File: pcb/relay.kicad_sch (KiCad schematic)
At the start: 14 parts, among them K1 PR24-5V-900-1A, P1 MountingHole_Pad, P2 MountingHole_Pad, P3 MountingHole_Pad, P4 MountingHole_Pad, Q1 MMBT3904, U3 LTV-356T

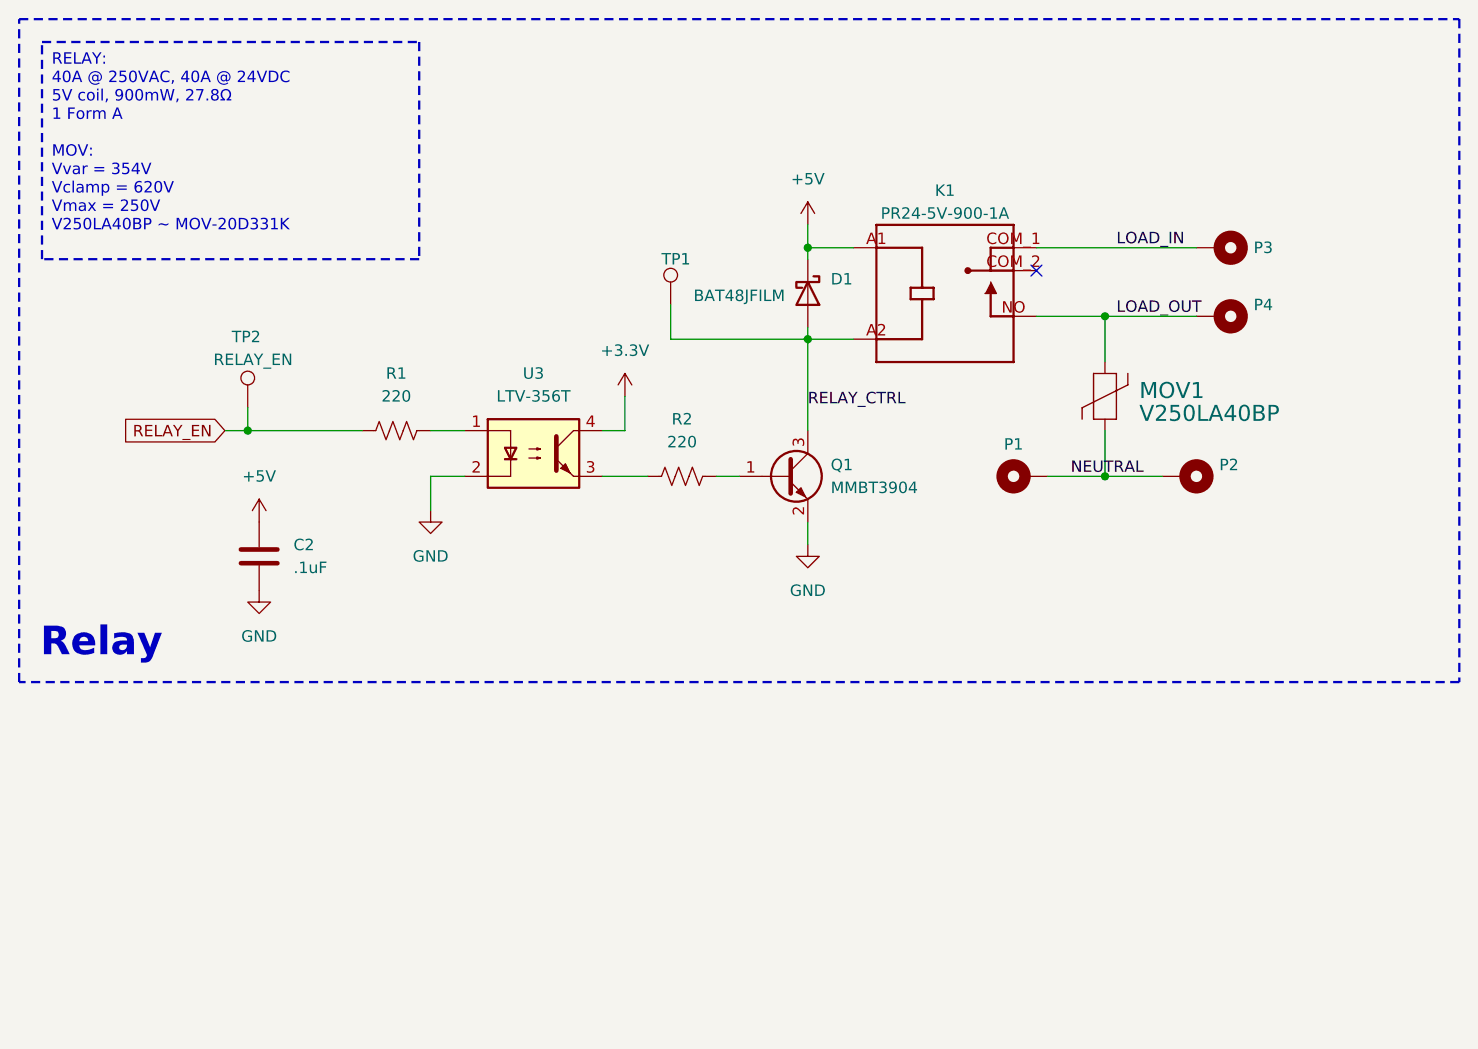
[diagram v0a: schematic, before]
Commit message: Updated to latest libraries
Changed to all CRG footprints (mostly)
Moved somethings around
Added LED jumper
Updated symbols/logos
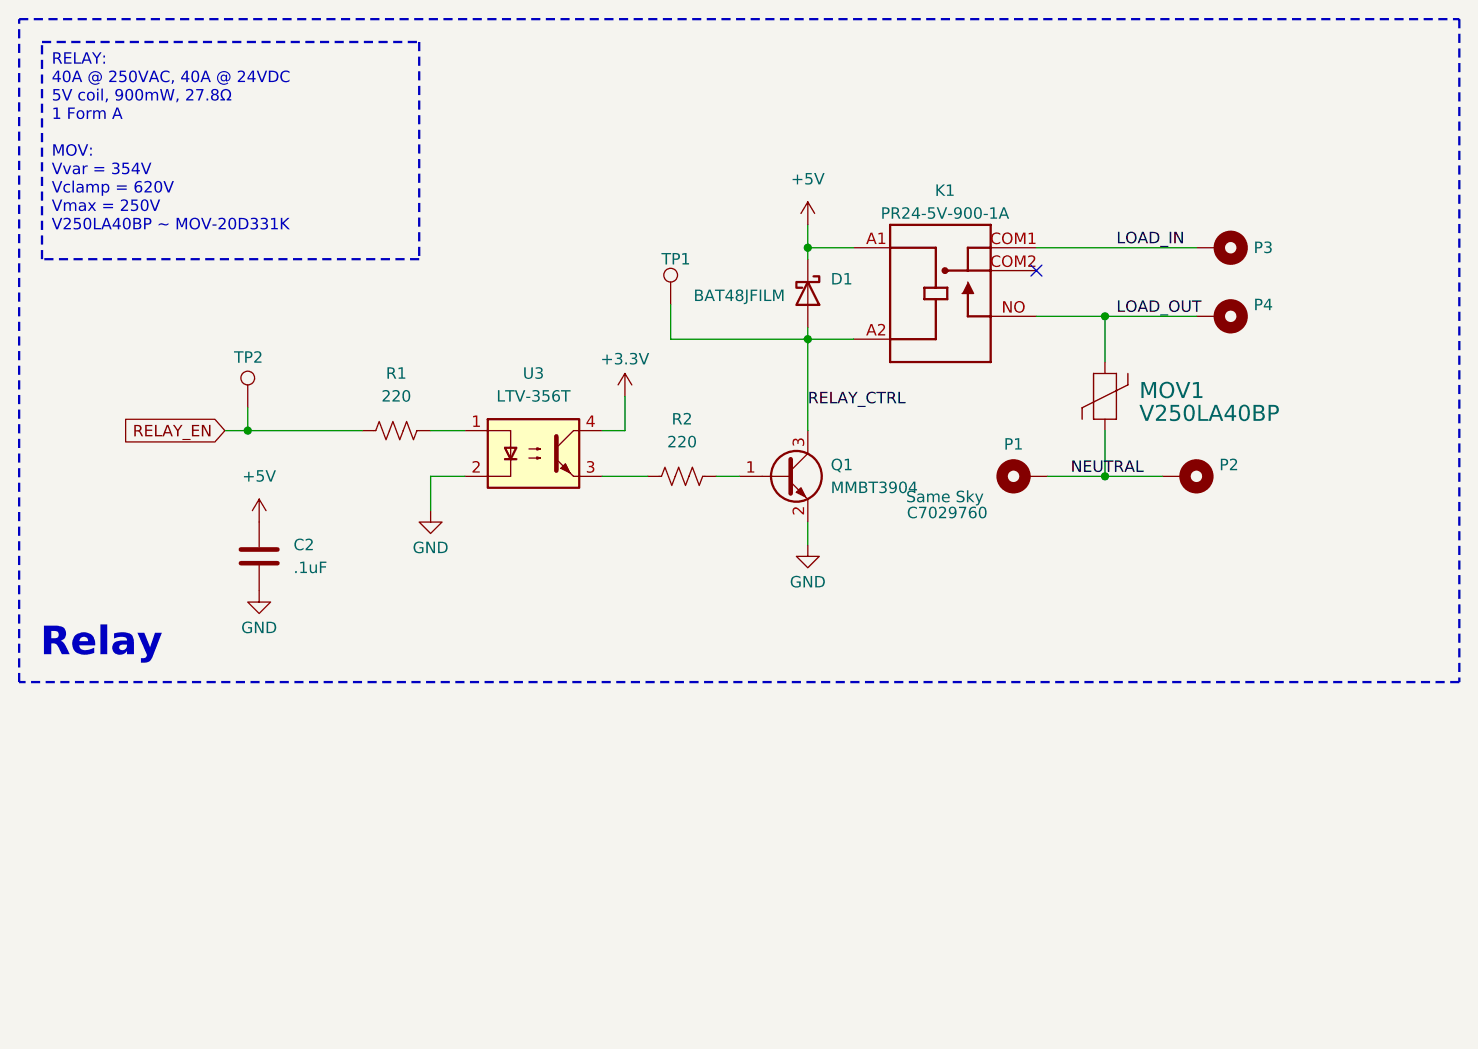
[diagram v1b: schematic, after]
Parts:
- C2: footprint Capacitor_SMD:C_0603_1608Metric -> CRGM Passive:C_0603_1608Metric; Digikey (none) -> 1276-1860-2-ND; Mouser (none) -> 187-CL10A105KB8NNNC
- D1: footprint Diode_SMD:D_SOD-323 -> CRG Makes:SOD-323; Digikey (none) -> 497-5711-2-ND; Mouser (none) -> 511-BAT48JFILM
- Q1: footprint Package_TO_SOT_SMD:SOT-23 -> CRGM Passive:SOT-23; Digikey (none) -> 3372-MMBT3904TR-ND; Mouser (none) -> 637-MMBT3904
- R1, R2: footprint Resistor_SMD:R_0603_1608Metric -> CRGM Passive:R_0603_1608Metric
- TP1: value RELAY_CTRL -> ~; symbol Connector:TestPoint -> CRGM Connector:TestPoint
- TP2: value RELAY_EN -> ~; symbol Connector:TestPoint -> CRGM Connector:TestPoint
- U3: Digikey (none) -> 160-1337-2-ND; Mouser (none) -> 859-LTV-356T
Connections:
- net LOAD_IN: now also K1.COM1; no longer K1.COM_1 (COM1)

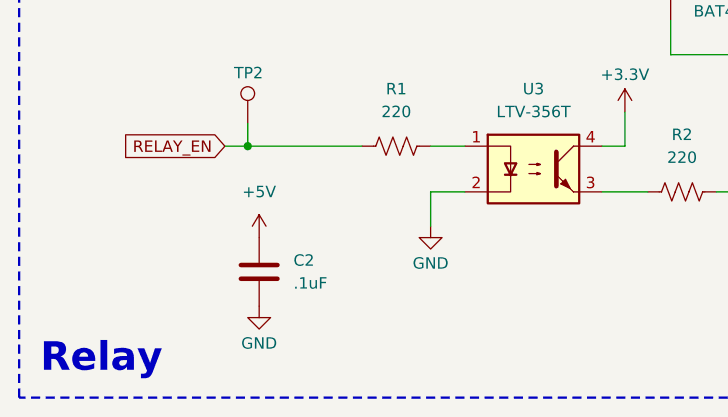
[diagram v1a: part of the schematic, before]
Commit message: Fixed capacitor attributes
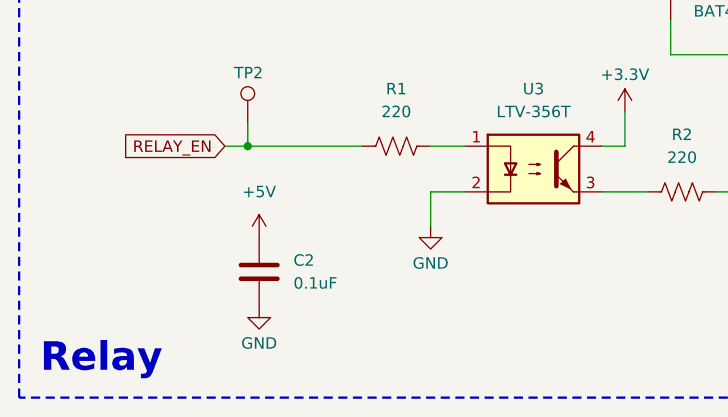
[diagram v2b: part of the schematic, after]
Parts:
- C2: value .1uF -> 0.1uF; Digikey 1276-1860-2-ND -> 1276-1005-2-ND; LCSC C15849 -> C66501; MPN CL10A105KB8NNNC -> CL10B104KO8NNNC; Mouser 187-CL10A105KB8NNNC -> 187-CL10B104KO8NNNC; Tolerance (none) -> 10%; Vr (none) -> 16V
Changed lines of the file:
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@@
 			)
 		)
-		(property "Value" ".1uF"
+		(property "Value" "0.1uF"
 			(at 45.72 76.1999 0)
 			(effects
@@
 			)
 		)
-		(property "MPN" "CL10A105KB8NNNC"
+		(property "MPN" "CL10B104KO8NNNC"
 			(at 41.91 74.93 0)
 			(effects
@@
 			)
 		)
-		(property "Digikey" "1276-1860-2-ND"
+		(property "LCSC" "C66501"
 			(at 41.91 74.93 0)
 			(effects
@@
 			)
 		)
-		(property "Mouser" "187-CL10A105KB8NNNC"
+		(property "Digikey" "1276-1005-2-ND"
 			(at 41.91 74.93 0)
 			(effects
@@
 			)
 		)
-		(property "LCSC" "C15849"
+		(property "Mouser" "187-CL10B104KO8NNNC"
 			(at 41.91 74.93 0)
 			(effects
@@
 			)
 		)
-		(property "Sim.Enable" ""
+		(property "Tolerance" "10%"
+			(at 41.91 74.93 0)
+			(effects
+				(font
+					(size 1.27 1.27)
+				)
+				(hide yes)
+			)
+		)
+		(property "Vr" "16V"
 			(at 41.91 74.93 0)
 			(effects
@@
 			)
 		)
-		(property "Sim.Enable" ""
-			(at 148.59 40.64 90)
-			(effects
-				(font
-					(size 1.27 1.27)
-				)
-				(hide yes)
-			)
-		)
 		(pin "1"
 		)
@@
 					(size 1.27 1.27)
 				)
-			)
-		)
-		(property "Sim.Enable" ""
-			(at 118.11 45.72 0)
-			(effects
-				(font
-					(size 1.27 1.27)
-				)
-				(hide yes)
 			)
 		)
@@
 			)
 		)
-		(property "Sim.Enable" ""
-			(at 72.39 63.5 0)
-			(effects
-				(font
-					(size 1.27 1.27)
-				)
-				(hide yes)
-			)
-		)
 		(pin "1"
 		)
@@
 			)
 		)
-		(property "Sim.Enable" ""
-			(at 135.89 57.15 0)
-			(effects
-				(font
-					(size 1.27 1.27)
-				)
-				(hide yes)
-			)
-		)
 		(pin "P$1"
 		)
@@
 		(property "Description" "Test Point D1.0mm"
 			(at 40.64 67.564 0)
-			(effects
-				(font
-					(size 1.27 1.27)
-				)
-				(hide yes)
-			)
-		)
-		(property "Sim.Enable" ""
-			(at 40.64 58.42 0)
 			(effects
 				(font
@@
 			)
 		)
-		(property "Sim.Enable" ""
-			(at 148.59 48.26 90)
-			(effects
-				(font
-					(size 1.27 1.27)
-				)
-				(hide yes)
-			)
-		)
 		(pin "1"
 		)
@@
 			)
 		)
-		(property "Sim.Enable" ""
-			(at 57.15 60.96 90)
-			(effects
-				(font
-					(size 1.27 1.27)
-				)
-				(hide yes)
-			)
-		)
 		(pin "2"
 		)
@@
 			)
 		)
-		(property "Sim.Enable" ""
-			(at 100.33 66.04 0)
-			(effects
-				(font
-					(size 1.27 1.27)
-				)
-				(hide yes)
-			)
-		)
 		(pin "3"
 		)
@@
 		(property "MN" "STMicroelectronics"
 			(at 102.87 45.72 0)
-			(effects
-				(font
-					(size 1.27 1.27)
-				)
-				(hide yes)
-			)
-		)
-		(property "Sim.Enable" ""
-			(at 102.87 45.72 90)
 			(effects
 				(font
@@
 			)
 		)
-		(property "Sim.Enable" ""
-			(at 88.9 66.04 90)
-			(effects
-				(font
-					(size 1.27 1.27)
-				)
-				(hide yes)
-			)
-		)
 		(pin "2"
 		)
@@
 			)
 		)
-		(property "Sim.Enable" ""
-			(at 127 66.04 90)
-			(effects
-				(font
-					(size 1.27 1.27)
-				)
-				(hide yes)
-			)
-		)
 		(pin "1"
 		)
@@
 			)
 		)
-		(property "Sim.Enable" ""
-			(at 144.78 66.04 90)
-			(effects
-				(font
-					(size 1.27 1.27)
-				)
-				(hide yes)
-			)
-		)
 		(pin "1"
 		)
@@
 			(effects
 				(font
-					(size 1.27 1.27)
-				)
-				(hide yes)
-			)
-		)
-		(property "Sim.Enable" ""
-			(at 87.63 46.99 0)
-			(effects
-				(font

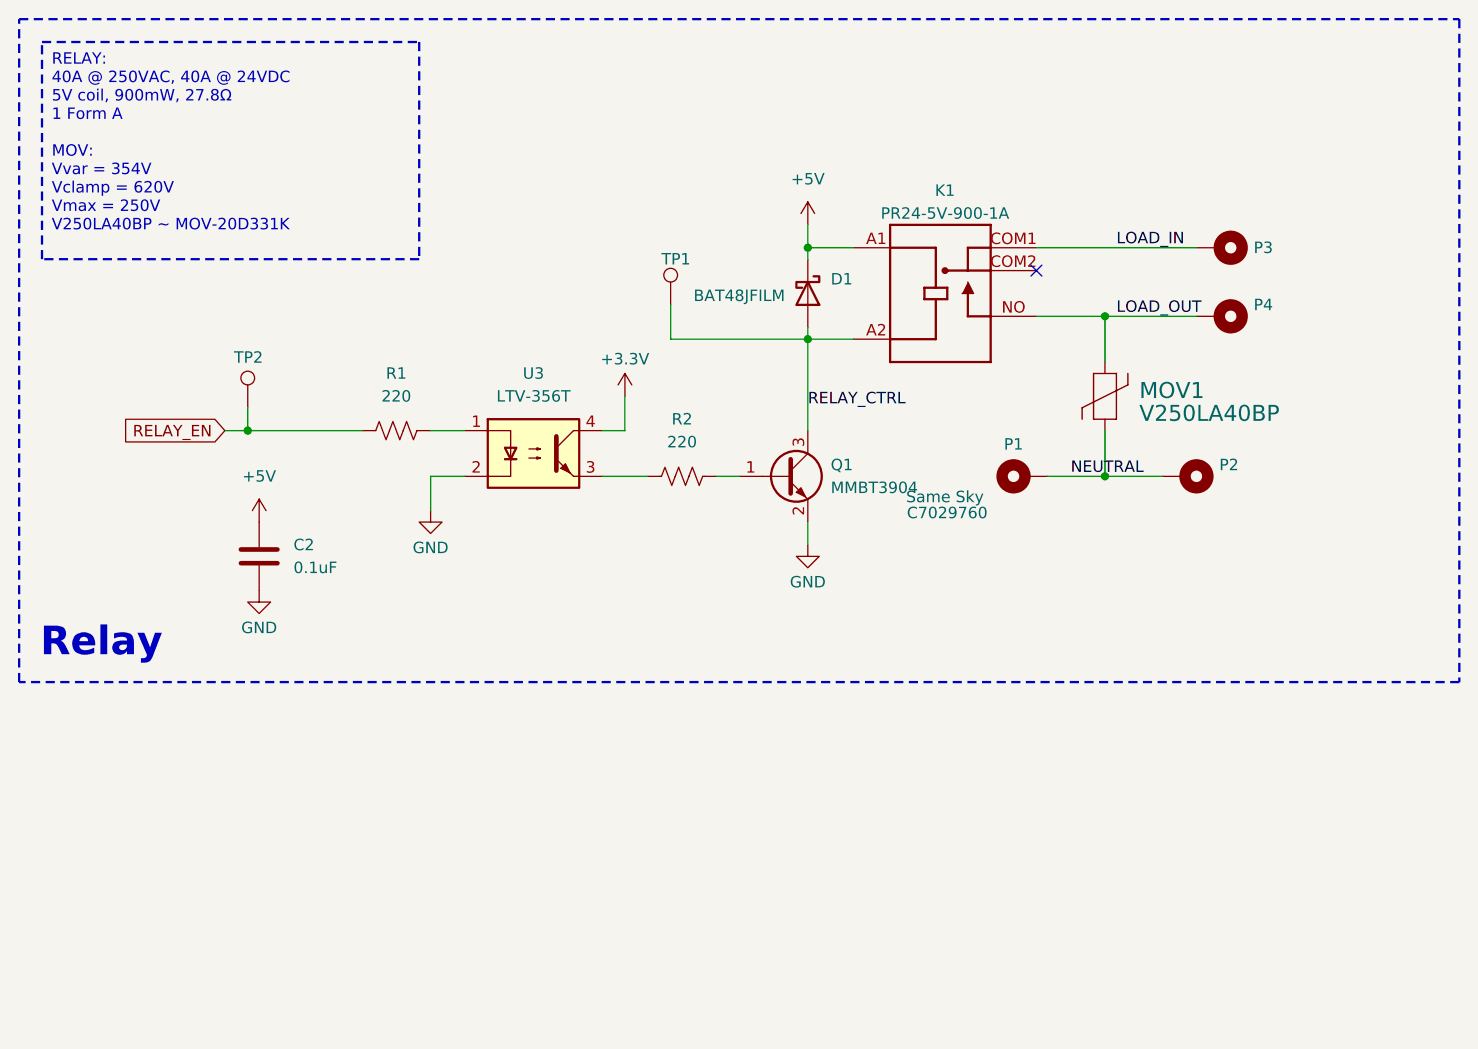
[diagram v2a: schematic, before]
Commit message: Updated for consistency
Updated footprints
Added ESD to power
Added second QWICC connector
Rerouted as required
Made mounting holes grounded
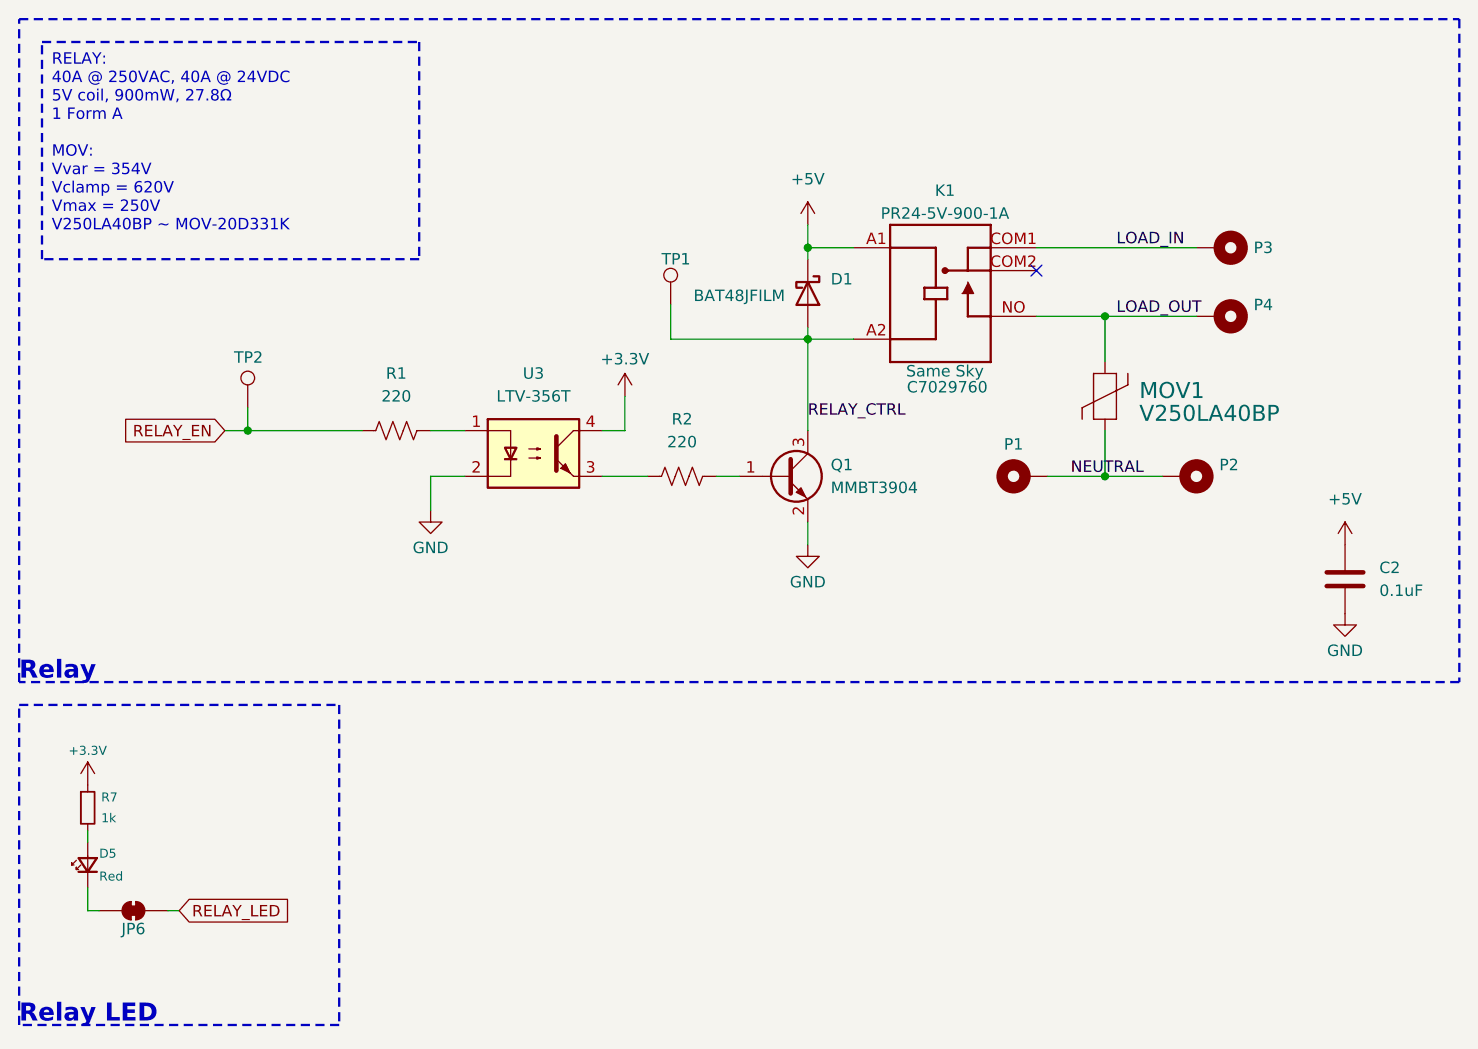
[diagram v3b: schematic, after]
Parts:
- added D5: Red, CRGM Passive:LED_0603_1608Metric, symbol Device:LED_Small
- added JP6: ~, CRGM Connector:SolderJumper-2_P1.3mm_Bridged_RoundedPad1.0x1.5mm, symbol CRGM Connector:SolderJumper_2_Bridged
- added R7: 1k, CRGM Passive:R_0603_1608Metric, symbol Device:R_Small
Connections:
- net +3.3V: now also R7.1
- new net: D5.1 (K), JP6.2 (B)
- new net: D5.2 (A), R7.2
- new net RELAY_LED: JP6.1 (A)
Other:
- note added: "Relay LED"
- moved on the sheet: C2
